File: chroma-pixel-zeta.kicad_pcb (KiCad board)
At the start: 4 copper layers, 138 x 93.2 mm, 151 parts, among them J1 Micro_SD_Card_Det_Hirose_DM3AT, J10 Conn_01x24_MountingPin, J11 AudioJack3, J12 USB_A, J14 LCD_TP_I2C, J15 LCD_SPI, J2 TFT_LCD, J3 2169900003, J4 SPI_LCD, J5 I2C-STEMMA-QT, J7 swd, J8 SPKR, J9 UART, SW1 SW_Push, SW2 SW_Push, SW3 SW_Push, SW4 SW_Push, U1 MT25Q, U10 PCM5102A, U11 TLV75733PDBV, U2 STM32H743IITx, U4 MT25Q, U5 TPS61169, U6 MAX98357AETE_, U7 CAT24C128, U8 TLV75733PDBV, U9 MT48LC16M16A2P, Y1 25MHz, Y2 32.768KHz

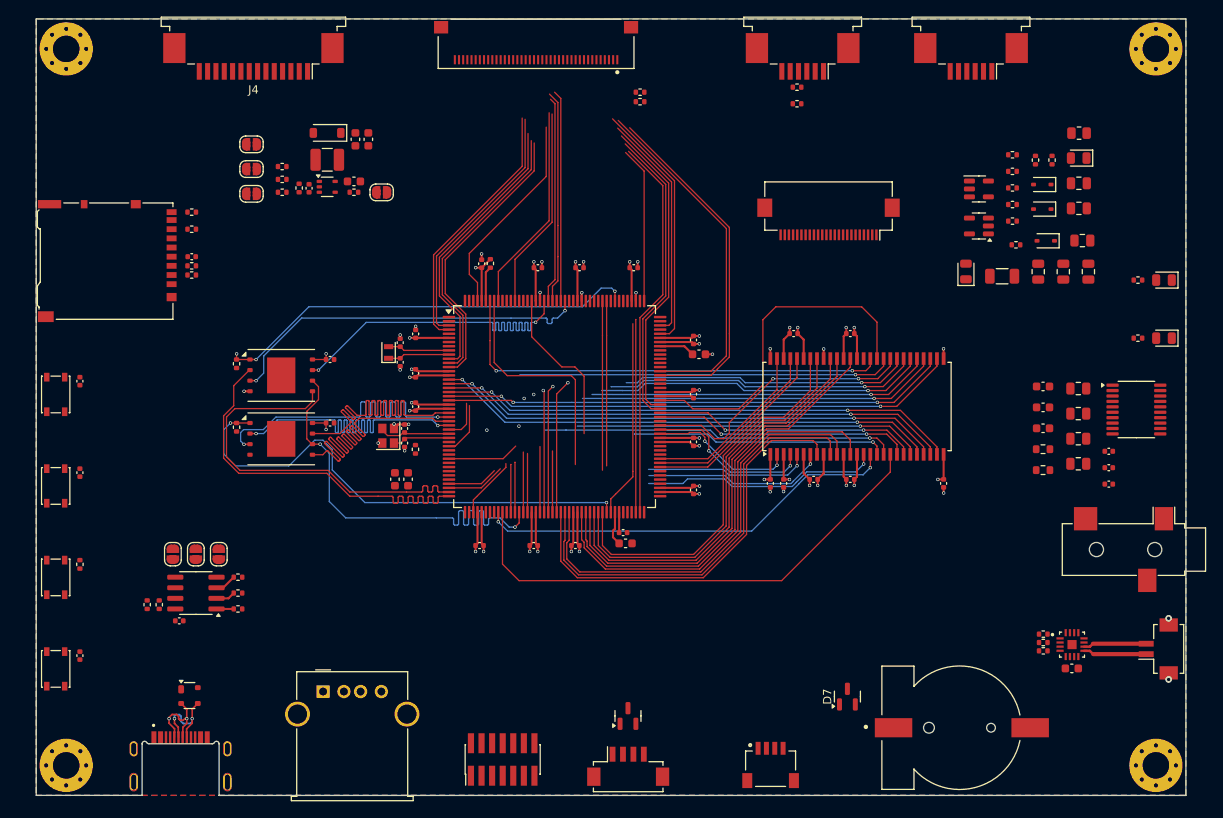
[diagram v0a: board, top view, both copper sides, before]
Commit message: Finished SDRAM, LTDC, QSPI, SDMMC, still an error on LTDC B channel
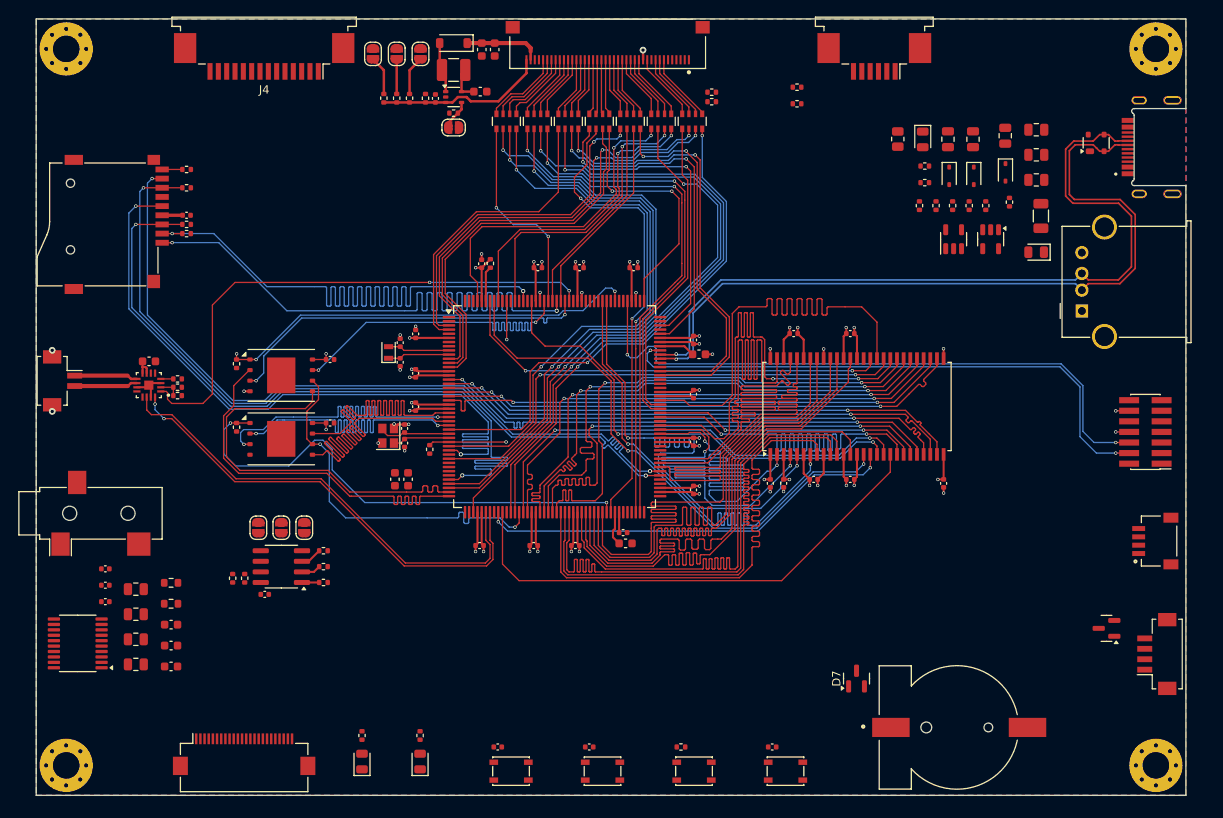
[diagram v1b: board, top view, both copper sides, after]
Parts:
- removed J1: Micro_SD_Card_Det_Hirose_DM3AT, Connector_Card:microSD_HC_Hirose_DM3AT-SF-PEJM5
- removed J15: LCD_SPI, Connector_FFC-FPC:TE_84952-6_1x06-1MP_P1.0mm_Horizontal
- added J6: Micro_SD_Card_Det1, TF-115:SD-TF-115, F.Cu at (90.1, 71.7)
- added RN1: 330, Resistor_SMD:R_Array_Convex_4x0603, F.Cu at (140.4, 59.3)
- added RN2: 330, Resistor_SMD:R_Array_Convex_4x0603, F.Cu at (136.7, 59.3)
- added RN3: 330, Resistor_SMD:R_Array_Convex_4x0603, F.Cu at (144.1, 59.3)
- added RN4: 330, Resistor_SMD:R_Array_Convex_4x0603, F.Cu at (147.8, 59.3)
- added RN5: 330, Resistor_SMD:R_Array_Convex_4x0603, F.Cu at (151.6, 59.3)
- added RN6: 330, Resistor_SMD:R_Array_Convex_4x0603, F.Cu at (155.3, 59.3)
- added RN7: 330, Resistor_SMD:R_Array_Convex_4x0603, F.Cu at (159.0, 59.3)
- moved J3 141.4 mm to (216.6, 62.4), turned to 90 degrees
- moved J8 135.4 mm to (83.4, 90.5), turned to -90 degrees
- moved U10 130.1 mm to (85.2, 122.0), turned to 180 degrees
- moved D2 127.5 mm to (207.5, 61.9), turned to 90 degrees
- moved J11 125.3 mm to (86.8, 106.4), turned to 90 degrees
- moved C55 121.8 mm to (88.5, 117.0), turned to 180 degrees
- moved C57 121.3 mm to (88.5, 115.0), turned to 180 degrees
- moved C59 120.9 mm to (88.5, 113.0), turned to 180 degrees
- moved C50 117.9 mm to (92.2, 124.5), turned to 180 degrees
- moved C23 116.7 mm to (93.8, 88.1), turned to 0 degrees
- moved C51 116.3 mm to (92.2, 121.5), turned to 180 degrees
- moved U6 115.1 mm to (93.8, 91.0), turned to 180 degrees
- moved C52 115.1 mm to (92.2, 118.5), turned to 180 degrees
- moved C53 114.1 mm to (92.2, 115.5), turned to 180 degrees
- moved C54 109.9 mm to (96.4, 124.8), turned to 180 degrees
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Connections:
- net /MEMORY SD CARD/SD_CMD renamed /MCU/SD_CMD
- net /MEMORY SD CARD/SD_DAT0 renamed /MCU/SD_DAT0
- net /MEMORY SD CARD/SD_DAT3 renamed /MCU/SD_DAT3
- J12 pad 2: unconnected-(J12-D--Pad2) -> /USB/USB_D-
- J12 pad 3: unconnected-(J12-D+-Pad3) -> /USB/USB_D+
- J12 pad 4: unconnected-(J12-GND-Pad4) -> GND
- J12 pad 5: unconnected-(J12-Shield-Pad5) -> GND
- J2 pad 11: /LCD/LTDC_CLK -> Net-(RN7-R4.1)
- J2 pad 13: /LCD/LTDC_B7 -> Net-(RN6-R1.1)
- J2 pad 14: /LCD/LTDC_B6 -> Net-(RN6-R2.1)
- J2 pad 15: /LCD/LTDC_B5 -> Net-(RN6-R3.1)
- J2 pad 16: /LCD/LTDC_B4 -> Net-(RN6-R4.1)
- J2 pad 17: /LCD/LTDC_B3 -> Net-(RN5-R1.1)
- J2 pad 18: /LCD/LTDC_B2 -> Net-(RN5-R2.1)
- J2 pad 19: /LCD/LTDC_B1 -> Net-(RN5-R3.1)
- J2 pad 20: /LCD/LTDC_B0 -> Net-(RN5-R4.1)
- J2 pad 21: /LCD/LTDC_G7 -> Net-(RN4-R1.1)
- J2 pad 22: /LCD/LTDC_G6 -> Net-(RN4-R2.1)
- J2 pad 23: /LCD/LTDC_G5 -> Net-(RN4-R3.1)
- J2 pad 24: /LCD/LTDC_G4 -> Net-(RN4-R4.1)
- J2 pad 25: /LCD/LTDC_G3 -> Net-(RN3-R1.1)
- J2 pad 26: /LCD/LTDC_G2 -> Net-(RN3-R2.1)
- J2 pad 27: /LCD/LTDC_G1 -> Net-(RN3-R3.1)
- J2 pad 28: /LCD/LTDC_G0 -> Net-(RN3-R4.1)
- J2 pad 29: /LCD/LTDC_R7 -> Net-(RN1-R1.1)
- J2 pad 30: /LCD/LTDC_R6 -> Net-(RN1-R2.1)
- J2 pad 31: /LCD/LTDC_R5 -> Net-(RN1-R3.1)
- J2 pad 32: /LCD/LTDC_R4 -> Net-(RN1-R4.1)
- J2 pad 33: /LCD/LTDC_R3 -> Net-(RN2-R1.1)
- J2 pad 34: /LCD/LTDC_R2 -> Net-(RN2-R2.1)
- J2 pad 35: /LCD/LTDC_R1 -> Net-(RN2-R3.1)
- J2 pad 36: /LCD/LTDC_R0 -> Net-(RN2-R4.1)
- J2 pad 7: /LCD/LTDC_DE -> Net-(RN7-R1.1)
- J2 pad 8: /LCD/LTDC_VSYNC -> Net-(RN7-R2.1)
- J2 pad 9: /LCD/LTDC_HSYNC -> Net-(RN7-R3.1)
- R10 pad 2: /MEMORY SD CARD/SD_DET -> /MCU/SD_DET
- R35 pad 2: /LCD/LCD_SCL -> /LCD/LCD_SDA
- R36 pad 2: /LCD/LCD_SDA -> /LCD/LCD_SCL
- U2 pad 154: /MEMORY SD CARD/SD_DAT2 -> /MCU/SD_DAT2
- U2 pad 33: /MEMORY SD CARD/SD_CLK -> /MCU/SD_CLK
- U2 pad 95: /MEMORY SD CARD/SD_DAT1 -> /MCU/SD_DAT1
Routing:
- net /MCU/SD_DAT3: track 0.00 -> 92.9 mm, vias 0 -> 2
- net /MCU/SD_CLK: track 0.00 -> 92.9 mm, vias 0 -> 2
- net /MCU/SD_DAT2: track 0.00 -> 92.9 mm, vias 0 -> 2
- net /MCU/SD_DAT1: track 0.00 -> 92.9 mm, vias 0 -> 2
- net /MCU/SD_CMD: track 0.00 -> 92.9 mm, vias 0 -> 2
- net /MCU/SD_DAT0: track 0.00 -> 92.9 mm, vias 0 -> 2
- net /USB/USB_D-: track 10.1 -> 93.6 mm, vias 2 -> 1
- net /MCU/BOOT0: track 0.00 -> 82.7 mm, vias 0 -> 1
- net /USB/USB_D+: track 10.9 -> 93.6 mm, vias 2 -> 1
- net /IO/DBG_SWCLK: track 0.00 -> 76.3 mm, vias 0 -> 2
- net /LCD/LTDC_R6: track 5.99 -> 77.4 mm, vias 0 -> 2
- net /LCD/LTDC_G1: track 5.75 -> 75.6 mm, vias 0 -> 2
- net /IO/DBG_SWDIO: track 0.00 -> 68.5 mm, vias 0 -> 2
- net /LCD/LTDC_R1: track 7.11 -> 72.9 mm, vias 0 -> 2
- net /LCD/LTDC_R2: track 6.10 -> 71.9 mm, vias 0 -> 2
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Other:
- outline, holes or cut-outs redrawn

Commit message: Finished SDRAM, QSPI, SDMMC, LTDC, TP, EEPROM, USB, debug (need to verify on UART)
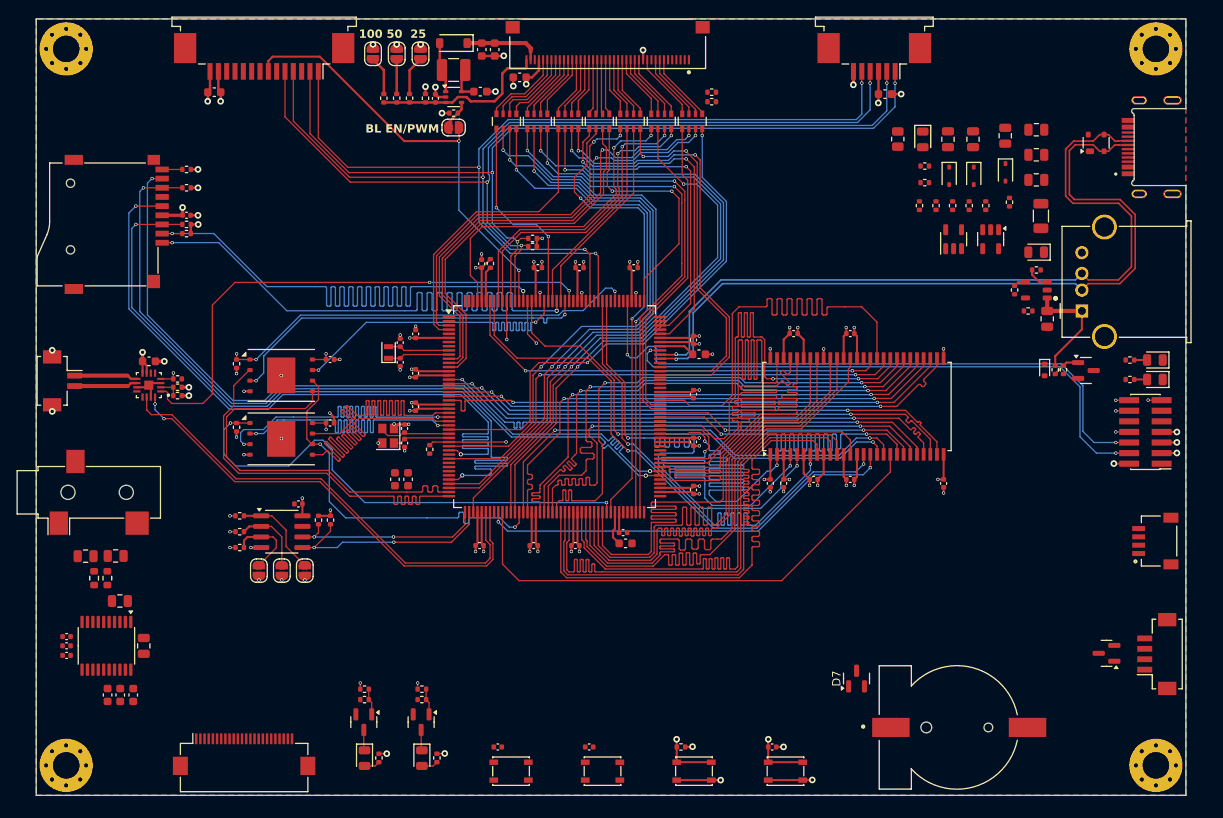
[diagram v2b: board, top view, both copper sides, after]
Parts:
- added C63: 4u7, Capacitor_SMD:C_0805_2012Metric, F.Cu at (201.6, 83.0)
- added C64: 10u, Capacitor_SMD:C_0603_1608Metric, F.Cu at (138.3, 54.1)
- added C65: 4u7, Capacitor_SMD:C_0603_1608Metric, F.Cu at (182.1, 56.1)
- added C66: 10u, Capacitor_SMD:C_0603_1608Metric, F.Cu at (101.6, 55.8)
- added D13: RED, LED_SMD:LED_0805_2012Metric, F.Cu at (214.5, 88.0)
- added D14: ESDALC6V1-1U2, Diode_SMD:D_SOD-523, F.Cu at (201.3, 89.2)
- added D15: GREEN, LED_SMD:LED_0805_2012Metric, F.Cu at (214.5, 90.3)
- added Q1: MMBT3904, Package_TO_SOT_SMD:SOT-23, F.Cu at (206.2, 89.2)
- added Q2: MMBT3904, Package_TO_SOT_SMD:SOT-23, F.Cu at (119.6, 131.4)
- added Q3: MMBT3904, Package_TO_SOT_SMD:SOT-23, F.Cu at (126.5, 131.4)
- added R42: 47K, Resistor_SMD:R_0402_1005Metric, F.Cu at (200.3, 77.2)
- added R43: 1K, Resistor_SMD:R_0402_1005Metric, F.Cu at (211.5, 88.0)
- added R44: 47K, Resistor_SMD:R_0402_1005Metric, F.Cu at (197.7, 79.6)
- added R45: 47K, Resistor_SMD:R_0402_1005Metric, F.Cu at (202.6, 89.1)
- added R46: 10K, Resistor_SMD:R_0402_1005Metric, F.Cu at (203.6, 89.1)
- added R47: 1K, Resistor_SMD:R_0402_1005Metric, F.Cu at (211.5, 90.3)
- added R48: 10K, Resistor_SMD:R_0402_1005Metric, F.Cu at (199.3, 82.1)
- added R49: 47K, Resistor_SMD:R_0402_1005Metric, F.Cu at (119.7, 127.5)
- added R50: 10K, Resistor_SMD:R_0402_1005Metric, F.Cu at (119.7, 128.7)
- added R51: 47K, Resistor_SMD:R_0402_1005Metric, F.Cu at (126.5, 127.5)
- added R52: 10K, Resistor_SMD:R_0402_1005Metric, F.Cu at (126.5, 128.7)
- added U12: STMPS2141STR, STMPS2141STR:SOT95P280X145-5N, F.Cu at (200.3, 79.6)
- moved R34 37.1 mm to (139.8, 74.3)
- moved R33 35.6 mm to (139.8, 73.4)
- moved R31 13.7 mm to (115.6, 107.2), turned to -90 degrees
- moved R5 12.8 mm to (104.7, 106.7), turned to 180 degrees
- moved C51 11.7 mm to (86.2, 111.5)
- moved C20 11.6 mm to (111.7, 105.3), turned to 180 degrees
- moved C58 11.4 mm to (88.8, 128.2), turned to -90 degrees
- moved R32 11.3 mm to (114.1, 107.2), turned to -90 degrees
- moved R6 10.9 mm to (104.7, 108.6), turned to 180 degrees
- moved R30 10.1 mm to (104.7, 110.5), turned to 180 degrees
- moved C59 9.37 mm to (83.9, 121.2)
- moved R38 9.26 mm to (87.2, 114.2), turned to 90 degrees
- moved C57 8.63 mm to (83.9, 122.3)
- moved C56 8.51 mm to (90.3, 128.2), turned to -90 degrees
- moved R37 8.24 mm to (88.8, 114.2), turned to 90 degrees
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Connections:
- D5 pad 1: GND -> Net-(D5-K)
- D6 pad 1: GND -> Net-(D6-K)
- J12 pad 1: unconnected-(J12-VBUS-Pad1) -> Net-(D14-K)
- J14 pad 1: GND -> /LCD/LCD_TP_SDA
- J14 pad 2: /LCD/LCD_TP_INT -> /LCD/LCD_TP_SCL
- J14 pad 3: /LCD/LCD_TP_RST -> +3V3
- J14 pad 4: +3V3 -> /LCD/LCD_TP_RST
- J14 pad 5: /LCD/LCD_TP_SCL -> /LCD/LCD_TP_INT
- J14 pad 6: /LCD/LCD_TP_SDA -> GND
- J4 pad 14: /LCD/LCD_VDD -> LCD_VDD
- J4 pad 7: /LCD/LED -> /LCD/LCD_BLK
- R23 pad 1: /MCU/LED_0 -> Net-(D5-A)
- R23 pad 2: Net-(D5-A) -> +3V3
- R24 pad 1: /MCU/LED_1 -> Net-(D6-A)
- R24 pad 2: Net-(D6-A) -> +3V3
- U2 pad 144: unconnected-(U2-PD2-Pad144) -> /LCD/LCD_TP_INT
- U2 pad 146: unconnected-(U2-PD4-Pad146) -> /LCD/LCD_TP_RST
- U2 pad 163: unconnected-(U2-PB5-Pad163) -> /LCD/LCD_BLK
- U2 pad 164: /LCD/LTDC_B6 -> /LCD/LCD_TP_SCL
- U2 pad 165: unconnected-(U2-PB7-Pad165) -> /LCD/LCD_TP_SDA
- U2 pad 167: unconnected-(U2-PB8-Pad167) -> /LCD/LTDC_B6
- U2 pad 45: unconnected-(U2-PH4-Pad45) -> /MEMORY EEPROM/SCL
- U2 pad 46: unconnected-(U2-PH5-Pad46) -> /MEMORY EEPROM/SDA
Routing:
- net /LCD/LCD_TP_RST: track 0.00 -> 113.4 mm, vias 0 -> 3
- net /LCD/LCD_TP_INT: track 0.00 -> 111.7 mm, vias 0 -> 3
- net /LCD/LCD_TP_SCL: track 0.00 -> 109.6 mm, vias 0 -> 3
- net /LCD/LCD_TP_SDA: track 0.00 -> 107.8 mm, vias 0 -> 3
- net /IO/DBG_SWO: track 1.61 -> 83.5 mm, vias 1 -> 2
- net /LCD/LCD_BLK: track 0.00 -> 52.4 mm, vias 0 -> 2
- net GND: track 82.8 -> 120.2 mm, vias 37 -> 66
- net +3V3: track 100.4 -> 131.5 mm, vias 22 -> 41
- net /MEMORY EEPROM/SDA: track 0.00 -> 26.2 mm, vias 0 -> 2
- net /MEMORY EEPROM/SCL: track 0.00 -> 23.3 mm, vias 0 -> 2
- net Net-(D14-K): track 0.00 -> 13.6 mm
- net VDD: track 6.84 -> 18.2 mm, vias 0 -> 2
- net /MCU/NRST: track 64.9 -> 74.7 mm, vias 2 -> 3
- net /MCU/BOOT0: track 82.7 -> 91.8 mm, vias 1 -> 2
- net Net-(JP5-A): track 2.07 -> 10.9 mm
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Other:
- board text added: "100"
- board text added: "25"
- board text added: "50"
- board text added: "BL EN/PWM"

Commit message: via changed to 0.3/0.5
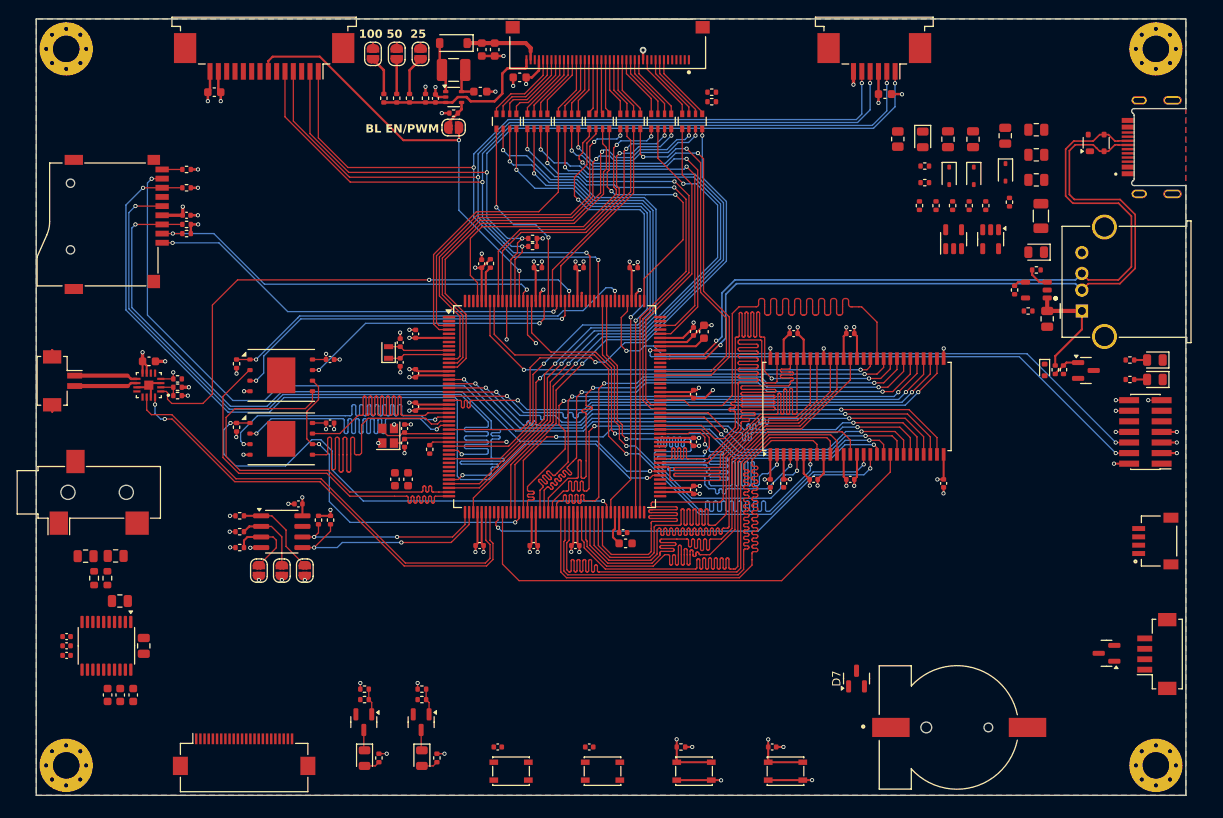
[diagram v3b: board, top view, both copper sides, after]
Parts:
- moved C34 2.78 mm to (160.4, 84.6), turned to 90 degrees
- moved C14 1.02 mm to (159.1, 84.6)
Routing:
- net /MCU/SD_DAT3: track 92.9 -> 49.3 mm
- net /MCU/SD_DAT2: track 92.9 -> 51.8 mm
- net /MEMORY SDRAM/SDRAM_BA0: track 60.9 -> 32.9 mm
- net /MCU/QUADSPI_BK2_IO3: track 44.9 -> 32.5 mm
- net /MCU/SD_DAT0: track 92.9 -> 103.2 mm
- net /MCU/SDRAM_ADD12: track 62.9 -> 70.6 mm
- net GND: track 120.2 -> 126.2 mm, vias 66 -> 58
- net /IO/DBG_SWCLK: track 76.3 -> 71.9 mm
- net /IO/DBG_SWDIO: track 68.5 -> 64.2 mm
- net /MCU/SD_DAT1: track 92.9 -> 88.6 mm
- net /MEMORY SDRAM/SDRAM_CLK: track 64.0 -> 67.6 mm
- net /MCU/QUADSPI_CLK: track 44.9 -> 41.8 mm
- net /MEMORY SDRAM/SDRAM_BA1: track 31.8 -> 34.1 mm
- net /MCU/SD_CLK: track 92.9 -> 90.8 mm
- net /MCU/SDRAM_ADD3: track 62.9 -> 64.9 mm
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
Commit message: not yet
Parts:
- added JP8: FLASH_CONFIG, Jumper:SolderJumper-3_P1.3mm_Open_RoundedPad1.0x1.5mm_NumberLabels, F.Cu at (105.9, 84.9)
- added JP9: FLASH_EN, Jumper:SolderJumper-2_P1.3mm_Open_RoundedPad1.0x1.5mm, F.Cu at (115.0, 84.9)
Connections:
- C22 pad 1: +3V3 -> Net-(JP9-A)
- R2 pad 2: /MCU/QUADSPI_BK2_NCS -> Net-(JP8-C)
- U4 pad 1: /MCU/QUADSPI_BK2_NCS -> Net-(JP8-C)
- U4 pad 8: +3V3 -> Net-(JP9-A)
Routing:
- net /MCU/SD_DAT3: track 49.3 -> 94.6 mm
- net /MCU/SD_DAT2: track 51.8 -> 90.4 mm
- net Net-(C34-Pad1): track 9.80 -> 43.4 mm, vias 0 -> 2
- net /MCU/BOOT0: track 91.8 -> 72.3 mm
- net /IO/DBG_SWDIO: track 64.2 -> 82.5 mm
- net /MCU/QUADSPI_BK1_NCS: track 59.7 -> 72.4 mm, vias 2 -> 3
- net /MEMORY SDRAM/SDRAM_UDQM: track 52.6 -> 64.8 mm
- net /MCU/QUADSPI_BK2_IO3: track 32.5 -> 44.7 mm
- net /IO/DBG_SWCLK: track 71.9 -> 82.8 mm
- net /MCU/SD_DAT0: track 103.2 -> 97.3 mm
- net /MCU/SDRAM_ADD12: track 70.6 -> 64.9 mm
- net Net-(JP8-C): track 0.00 -> 4.67 mm
- net /MCU/QUADSPI_BK2_NCS: track 50.4 -> 46.2 mm
- net Net-(JP9-A): track 0.00 -> 4.04 mm
- net /MCU/NRST: track 74.7 -> 70.8 mm
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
